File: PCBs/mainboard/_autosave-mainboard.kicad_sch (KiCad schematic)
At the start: 25 parts, among them J1 USB_C_Receptacle_USB2.0_16P, SW1 SW_Push_Dual, SW2 SW_Push_Dual, U3 ESP32-S3-WROOM-1

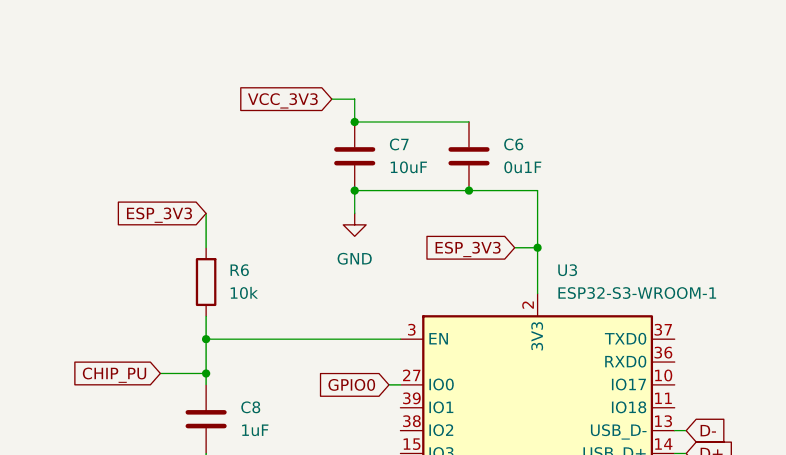
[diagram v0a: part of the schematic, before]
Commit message: Added ESP32 to Schematic
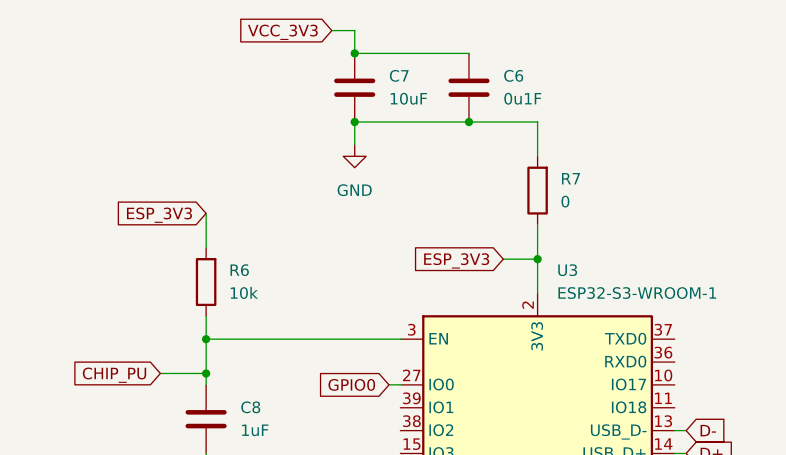
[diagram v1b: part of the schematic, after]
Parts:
- added R7: 0, symbol Device:R
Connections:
- net GND: now also R7.2; no longer R6.2, U3.2 (3V3)
- new net ESP_3V3: R6.2, R7.1, U3.2 (3V3)
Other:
- moved on the sheet: C6, C7
